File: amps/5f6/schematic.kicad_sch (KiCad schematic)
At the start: 69 parts, among them T3 2R sec

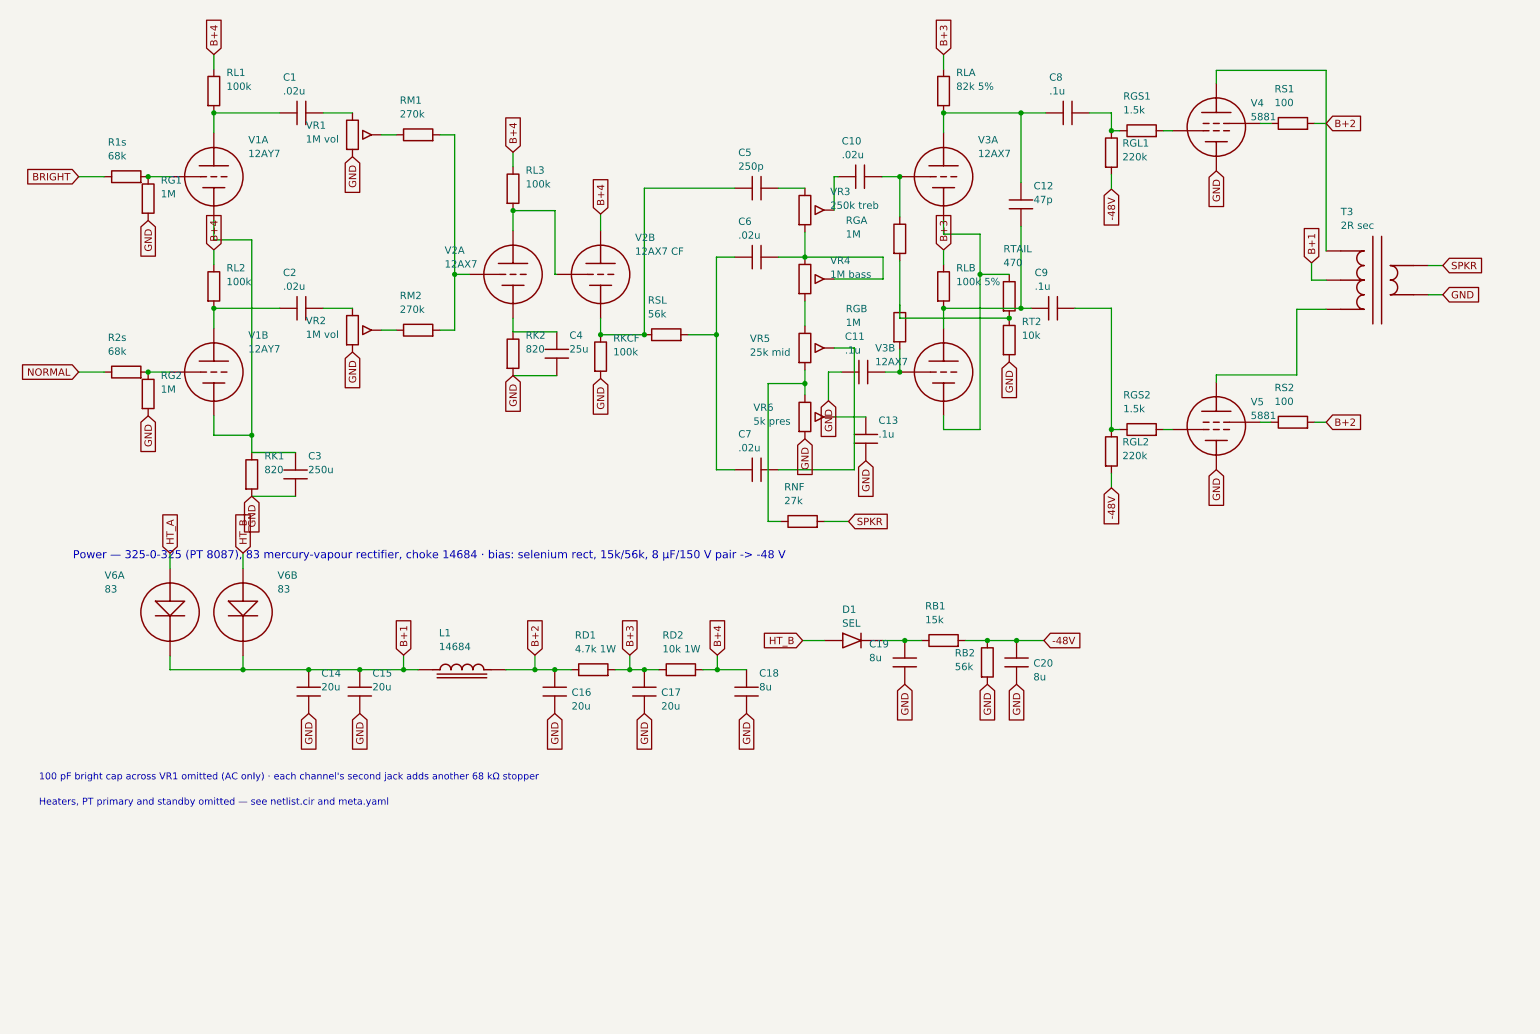
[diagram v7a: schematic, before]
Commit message: Add: real tube pin numbers and readable valve glyphs on every schematic
Phase B of the drawing program. A factory service sheet numbers every tube
pin, because the number is what a technician puts a probe on. This corpus
printed none, and the numbers hidden in its symbols were positional
placeholders (P=1, G=2, K=3) that would have published a 6V6GT's plate as
pin 1 when it is pin 3.

1055 electrodes now carry the real number, 1027 lettered (27 are shared
filaments deduped, 1 dropped for want of clear space on the 6G2). Resolved per
instance from reference/tubes/<slug>.yaml through the same alias resolution the
layout renderer uses, so a 12AX7 section and a 6SL7 section each get their own
basing. A valve whose basing the corpus does not carry prints nothing rather
than a wrong number.

Section letters and basing units are now separate things, which cost a detour
worth recording. The RCA 12AX7-A sheet reads "Pin 1 - Plate of Unit No.2 ...
Pin 6 - Plate of Unit No.1", so unit numbering is not pin order; the 5Y3 and
GZ34 number their units in opposite pin order, so nothing positional can
express it. But the section LETTER is a designator, not a basing fact: this
corpus, like every technician, calls the first stage in signal order V1A, and
five amps' prose already did. On four amps the factory sheets put that first
stage on the other half -- the AA764's own schematic prints +200 V on pin 1 --
so those drawings now state their unit explicitly, each citing its source, and
no letter, netlist, parts list or layout comment changed. 183 layout comments
agree with the printed numbers, 0 disagree. A guard fires if two halves of one
bottle resolve to the same unit, which is exactly how this was found.

Glyphs: the cathode gains a bracket and filament hairpin so it can no longer be
confused with the plate bar, the pentode's screen sits on its own row, and a
rectifier draws as one envelope over its sections instead of two apparent
bottles. Line weights are scaled per sheet to a co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
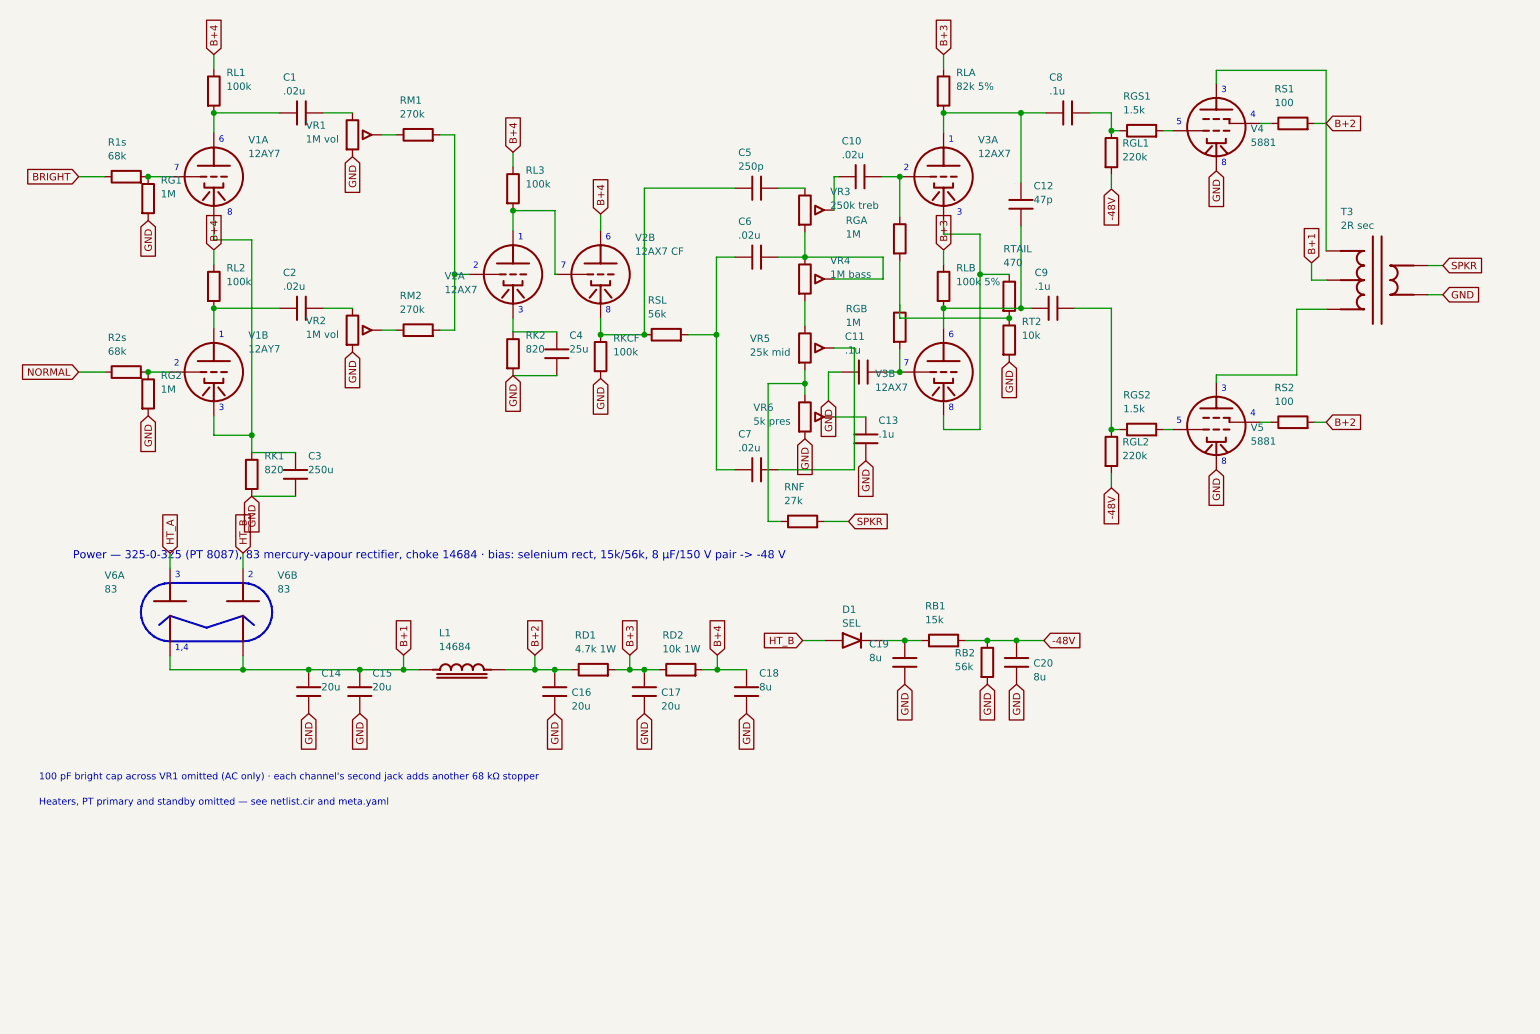
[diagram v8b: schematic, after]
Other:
- note added: "1"
- note added: "1,4"
- note added: "2"
- note added: "3"
- note added: "4"
- note added: "5"
- note added: "6"
- note added: "7"
- note added: "8"
